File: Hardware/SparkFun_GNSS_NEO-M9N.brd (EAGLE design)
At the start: 64.9 x 38 mm, 68 parts, among them J1 MICROMOD_STANDARD, U1 U-BLOX_NEO-M9N, U2 3.3V, U3 EEPROM, U4 74HC1G04

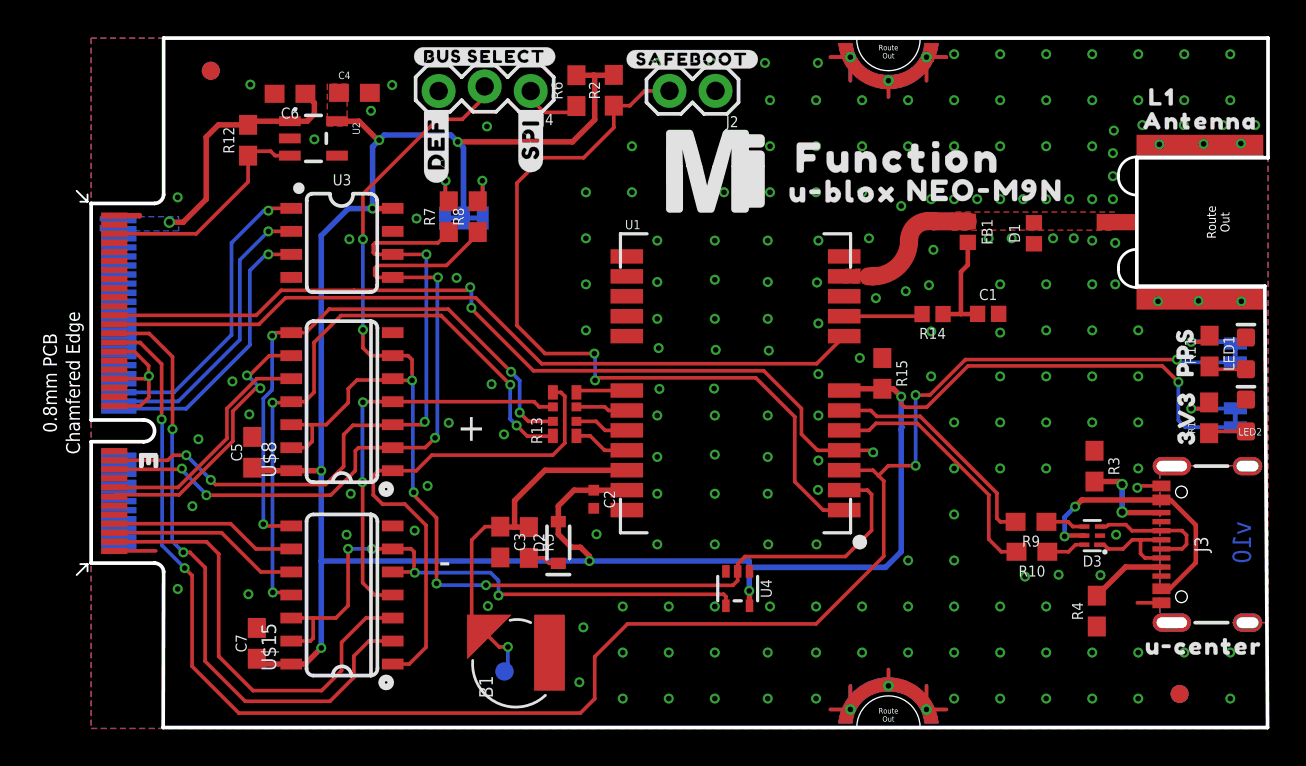
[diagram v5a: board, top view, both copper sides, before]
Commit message: Adds more text to clarify selection jumper, fixes some clearance issues and wire stubs
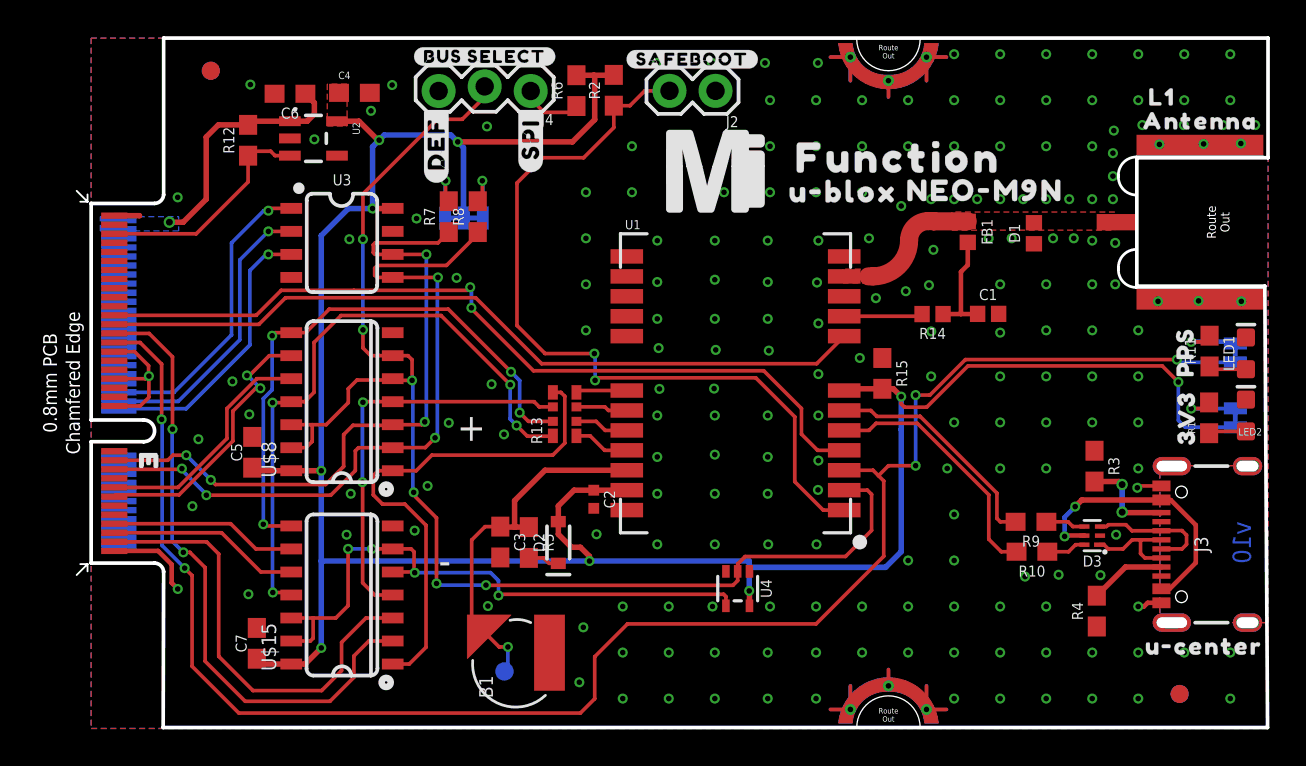
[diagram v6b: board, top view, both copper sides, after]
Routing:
- net GND: track 19.7 -> 22.4 mm, vias 205 -> 206
- net INT: track 48.0 -> 46.2 mm, vias 3 -> 2
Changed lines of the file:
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@@
 <layer number="115" name="ReferenceISLANDS" color="7" fill="1" visible="no" active="no"/>
 <layer number="116" name="Patch_BOT" color="9" fill="4" visible="no" active="no"/>
-<layer number="117" name="PM_Ref" color="26" fill="1" visible="no" active="yes"/>
+<layer number="117" name="PM_Ref" color="26" fill="1" visible="yes" active="yes"/>
 <layer number="118" name="Rect_Pads" color="7" fill="1" visible="no" active="no"/>
-<layer number="119" name="PF_Ref" color="31" fill="1" visible="no" active="yes"/>
-<layer number="120" name="WFL_Ref" color="25" fill="1" visible="no" active="yes"/>
+<layer number="119" name="PF_Ref" color="31" fill="1" visible="yes" active="yes"/>
+<layer number="120" name="WFL_Ref" color="25" fill="1" visible="yes" active="yes"/>
 <layer number="121" name="_tsilk" color="7" fill="1" visible="no" active="no"/>
 <layer number="122" name="_bsilk" color="7" fill="1" visible="no" active="no"/>
@@
 <wire x1="25.781" y1="11.413" x2="25.781" y2="12.281" width="0.3048" layer="1"/>
 <wire x1="25.781" y1="12.281" x2="26.6492" y2="13.1492" width="0.3048" layer="1"/>
-<wire x1="44.8283" y1="16.6243" x2="44.704" y2="16.5" width="0.2032" layer="16"/>
 <wire x1="12.7" y1="14.224" x2="12.7" y2="27.2" width="0.3048" layer="16"/>
 <wire x1="14.192" y1="28.692" x2="15.53" y2="28.692" width="0.3048" layer="16"/>
@@
 <wire x1="57.835" y1="13.385" x2="57.7342" y2="13.2842" width="0.2032" layer="1"/>
 <wire x1="59.0648" y1="6.935" x2="59.064" y2="6.9342" width="0.2032" layer="1"/>
-<wire x1="59.064" y1="6.9342" x2="57.7342" y2="6.9342" width="0.2032" layer="1"/>
 <via x="31.2166" y="36.7284" extent="1-16" drill="0.3048"/>
 <via x="40.005" y="4.191" extent="1-16" drill="0.3048"/>
@@
 <contactref element="C7" pad="2"/>
 <via x="8.727" y="17.3344" extent="1-16" drill="0.3048"/>
-<wire x1="1.275" y1="9.8" x2="3.5684" y2="9.8" width="0.2032" layer="1"/>
 <via x="8.679" y="7.4094" extent="1-16" drill="0.3048"/>
 <via x="37.398" y="20.852" extent="1-16" drill="0.3048"/>
@@
 <via x="52.705" y="6.731" extent="1-16" drill="0.3048"/>
 <via x="42.545" y="6.731" extent="1-16" drill="0.3048"/>
-<via x="47.625" y="14.351" extent="1-16" drill="0.3048"/>
+<via x="47.244" y="14.351" extent="1-16" drill="0.3048"/>
 <via x="47.625" y="16.891" extent="1-16" drill="0.3048"/>
 <via x="50.165" y="16.891" extent="1-16" drill="0.3048"/>
@@
 <via x="40.005" y="6.731" extent="1-16" drill="0.3048"/>
 <via x="37.465" y="6.731" extent="1-16" drill="0.3048"/>
-<via x="34.417" y="6.731" extent="1-16" drill="0.3048"/>
+<via x="34.29" y="6.731" extent="1-16" drill="0.3048"/>
 <via x="31.877" y="1.651" extent="1-16" drill="0.3048"/>
 <via x="31.877" y="4.191" extent="1-16" drill="0.3048"/>
@@
 <via x="27.305" y="24.511" extent="1-16" drill="0.3048"/>
 <via x="27.305" y="21.971" extent="1-16" drill="0.3048"/>
+<via x="57.785" y="6.731" extent="1-16" drill="0.3048"/>
+<wire x1="59.0648" y1="6.935" x2="58.3028" y2="6.935" width="0.254" layer="1"/>
+<wire x1="58.3028" y1="6.935" x2="58.0988" y2="6.731" width="0.254" layer="1"/>
+<wire x1="58.0988" y1="6.731" x2="57.785" y2="6.731" width="0.254" layer="1"/>
+<wire x1="4.779" y1="7.6994" x2="4.445" y2="8.0334" width="0.254" layer="1"/>
+<wire x1="4.445" y1="9.0504" x2="3.6954" y2="9.8" width="0.254" layer="1"/>
+<wire x1="4.445" y1="8.0334" x2="4.445" y2="9.0504" width="0.254" layer="1"/>
+<wire x1="3.6954" y1="9.8" x2="1.275" y2="9.8" width="0.254" layer="1"/>
 </signal>
 <signal name="SCL/SCK">
 <contactref element="R13" pad="P6"/>
-<wire x1="25.4502" y1="17.78" x2="25.482" y2="17.7482" width="0.2032" layer="1"/>
 <contactref element="U$8" pad="4"/>
 <contactref element="U$15" pad="4"/>
@@
 <contactref element="U1" pad="8"/>
 <contactref element="J1" pad="51"/>
-<wire x1="41.56" y1="21.65" x2="41.627" y2="21.717" width="0.2032" layer="1"/>
 <wire x1="1.275" y1="22.3" x2="9.26" y2="22.3" width="0.2032" layer="1"/>
 <wire x1="9.26" y1="22.3" x2="10.73" y2="23.77" width="0.2032" layer="1"/>
@@
 <signal name="INT">
 <contactref element="U1" pad="4"/>
-<wire x1="43.307" y1="15.0876" x2="43.1546" y2="15.24" width="0.2032" layer="16"/>
-<via x="43.1546" y="15.24" extent="1-16" drill="0.3048"/>
 <contactref element="J1" pad="53"/>
-<wire x1="41.56" y1="15.35" x2="43.0446" y2="15.35" width="0.2032" layer="1"/>
-<wire x1="43.0446" y1="15.35" x2="43.1546" y2="15.24" width="0.2032" layer="1"/>
 <wire x1="1.275" y1="22.8" x2="9.11" y2="22.8" width="0.2032" layer="1"/>
 <wire x1="9.11" y1="22.8" x2="10.49" y2="24.18" width="0.2032" layer="1"/>
@@
 <wire x1="47.014" y1="22.87" x2="48" y2="22.87" width="0.254" layer="1"/>
 <wire x1="48" y1="22.87" x2="48.9116" y2="22.87" width="0.254" layer="1"/>
-<wire x1="48.3774" y1="26.8264" x2="48.482" y2="26.7218" width="0.254" layer="1"/>
 <wire x1="48.9216" y1="22.88" x2="48.9116" y2="22.87" width="0.254" layer="1"/>
 <wire x1="48.3774" y1="25.5774" x2="48.3774" y2="26.8264" width="0.254" layer="1"/>
@@
 <wire x1="23.368" y1="12.573" x2="23.368" y2="11.113" width="0.3048" layer="1"/>
 <wire x1="25.045" y1="14.25" x2="23.368" y2="12.573" width="0.3048" layer="1"/>
-<wire x1="22.5806" y1="11.1384" x2="22.719" y2="11.2768" width="0.3048" layer="1"/>
 <wire x1="21.4122" y1="5.6034" x2="21" y2="6.0156" width="0.2032" layer="1"/>
 <wire x1="21" y1="6.0156" x2="21" y2="10.4" width="0.2032" layer="1"/>
@@
 <wire x1="16.737" y1="19.21" x2="16.717" y2="19.23" width="0.2032" layer="1"/>
 <wire x1="16.717" y1="19.23" x2="16.643" y2="19.304" width="0.2032" layer="1"/>
-<wire x1="16.643" y1="20.56" x2="16.643" y2="20.574" width="0.2032" layer="1"/>
 <wire x1="11.043" y1="16.764" x2="12.2" y2="16.764" width="0.2032" layer="1"/>
 <wire x1="12.2" y1="16.764" x2="12.974" y2="16.764" width="0.2032" layer="1"/>
@@
 <wire x1="18.44" y1="15.5" x2="18.98" y2="16.04" width="0.2032" layer="1"/>
 <via x="18.98" y="16.04" extent="1-16" drill="0.3048"/>
-<wire x1="21.4308" y1="27.3" x2="21.3936" y2="27.3372" width="0.2032" layer="1"/>
 <wire x1="21.3936" y1="27.3372" x2="21.336" y2="27.3948" width="0.2032" layer="1"/>
 <wire x1="18.98" y1="16.04" x2="19.107" y2="16.167" width="0.2032" layer="16"/>
@@
 <via x="18.41" y="16.92" extent="1-16" drill="0.3048"/>
 <wire x1="18.41" y1="16.92" x2="18.5" y2="17.01" width="0.2032" layer="16"/>
-<wire x1="19.5" y1="27.5" x2="19.6705" y2="27.3295" width="0.2032" layer="1"/>
 <wire x1="18.5" y1="26.159" x2="18.503" y2="26.162" width="0.2032" layer="16"/>
 <via x="18.503" y="26.162" extent="1-16" drill="0.3048"/>
@@
 <via x="14.18" y="9.91" extent="1-16" drill="0.3048"/>
 <wire x1="12.25" y1="6.096" x2="13.5" y2="6.096" width="0.2032" layer="1"/>
-<wire x1="15.48" y1="9.91" x2="15.5" y2="9.91" width="0.2032" layer="1"/>
 <wire x1="15.5" y1="9.91" x2="16.639" y2="9.91" width="0.2032" layer="1"/>
 <wire x1="16.639" y1="9.91" x2="16.643" y2="9.906" width="0.2032" layer="1"/>

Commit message: Adds some vias, moves some silk
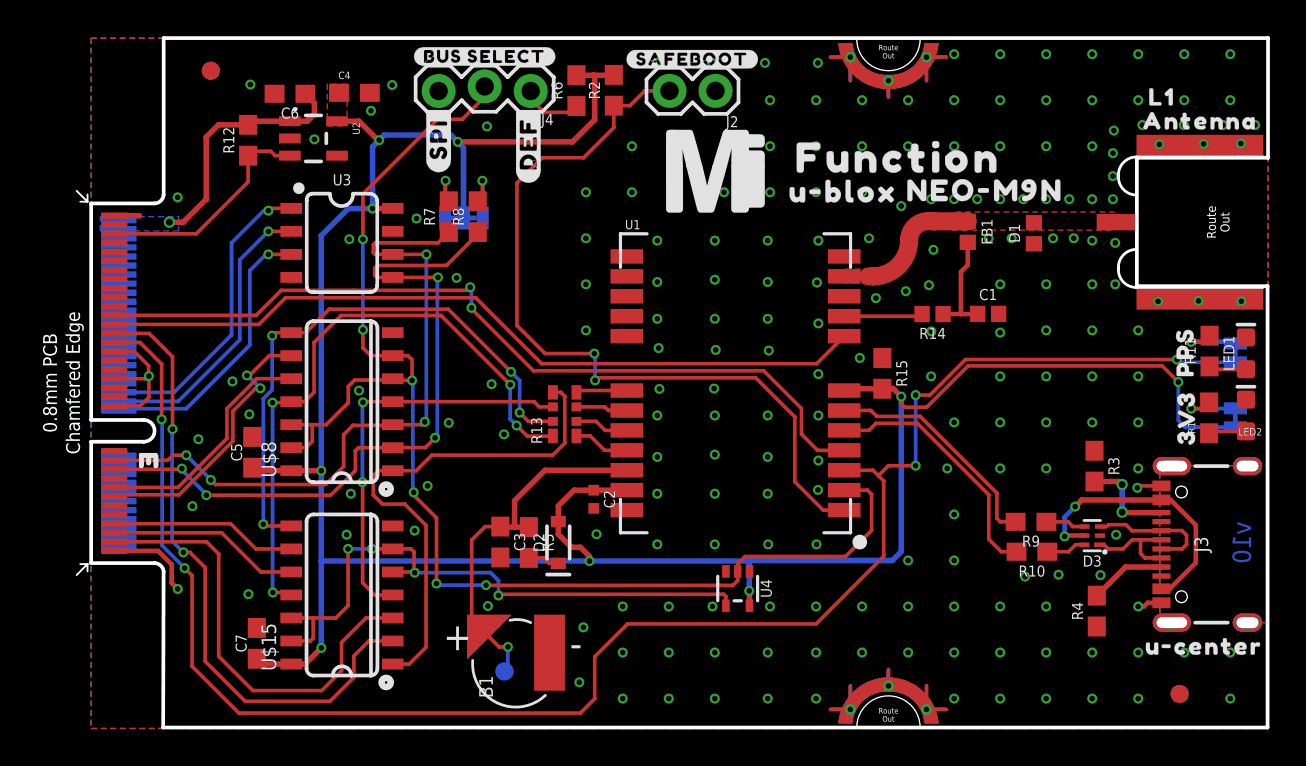
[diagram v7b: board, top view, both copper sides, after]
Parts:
- moved U$17 5.08 mm to (19.2, 32.5)
- moved U$16 5.08 mm to (24.1, 32.3)
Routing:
- net GND: vias 206 -> 207
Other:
- outline, holes or cut-outs redrawn
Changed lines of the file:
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@@
 <?xml version="1.0" encoding="utf-8"?>
 <!DOCTYPE eagle SYSTEM "eagle.dtd">
-<eagle version="9.6.2">
+<eagle version="9.5.1">
 <drawing>
 <settings>
@@
 <layer number="45" name="Holes" color="7" fill="1" visible="yes" active="yes"/>
 <layer number="46" name="Milling" color="3" fill="1" visible="no" active="yes"/>
-<layer number="47" name="Measures" color="7" fill="1" visible="no" active="yes"/>
+<layer number="47" name="Measures" color="7" fill="1" visible="yes" active="yes"/>
 <layer number="48" name="Document" color="7" fill="1" visible="no" active="yes"/>
 <layer number="49" name="Reference" color="13" fill="1" visible="yes" active="yes"/>
@@
 <layer number="115" name="ReferenceISLANDS" color="7" fill="1" visible="no" active="no"/>
 <layer number="116" name="Patch_BOT" color="9" fill="4" visible="no" active="no"/>
-<layer number="117" name="PM_Ref" color="26" fill="1" visible="yes" active="yes"/>
+<layer number="117" name="PM_Ref" color="26" fill="1" visible="no" active="yes"/>
 <layer number="118" name="Rect_Pads" color="7" fill="1" visible="no" active="no"/>
-<layer number="119" name="PF_Ref" color="31" fill="1" visible="yes" active="yes"/>
-<layer number="120" name="WFL_Ref" color="25" fill="1" visible="yes" active="yes"/>
+<layer number="119" name="PF_Ref" color="31" fill="1" visible="no" active="yes"/>
+<layer number="120" name="WFL_Ref" color="25" fill="1" visible="no" active="yes"/>
 <layer number="121" name="_tsilk" color="7" fill="1" visible="no" active="no"/>
 <layer number="122" name="_bsilk" color="7" fill="1" visible="no" active="no"/>
@@
 <wire x1="64.9478" y1="31.496" x2="57.7088" y2="31.496" width="0.2032" layer="20"/>
 <wire x1="57.7088" y1="31.496" x2="57.7088" y2="24.4094" width="0.2032" layer="20"/>
-<wire x1="57.7088" y1="24.4094" x2="64.77" y2="24.4094" width="0.2032" layer="20"/>
+<wire x1="57.7088" y1="24.4094" x2="64.9224" y2="24.4094" width="0.2032" layer="20"/>
 <wire x1="64.9478" y1="31.496" x2="64.9478" y2="38.1" width="0.2032" layer="20"/>
-<wire x1="64.77" y1="24.4094" x2="64.9224" y2="0.0508" width="0.2032" layer="20"/>
+<wire x1="64.9224" y1="24.4094" x2="64.9224" y2="0.0508" width="0.2032" layer="20"/>
 <text x="88.5" y="40" size="1.778" layer="51" font="vector" ratio="15">0.8mm PCB
 45 degree chamfered edge
@@
 <dimension x1="64.9424" y1="27.94" x2="64.9478" y2="38.1" x3="74.673896875" y3="33.014828125" textsize="1.778" textratio="15" layer="47" unit="inch"/>
 <text x="64.008" y="11.43" size="1.016" layer="16" font="vector" ratio="15" rot="SMR270">v10</text>
-<text x="20.193" y="15.875" size="1.524" layer="21" font="vector" ratio="15">+</text>
-<text x="19.177" y="8.509" size="1.524" layer="21" font="vector" ratio="15">-</text>
+<text x="19.431" y="4.318" size="1.524" layer="21" font="vector" ratio="15">+</text>
+<text x="26.416" y="3.937" size="1.524" layer="21" font="vector" ratio="15">-</text>
 <dimension x1="58.7248" y1="10.16" x2="58.674" y2="0" x3="72.161125" y3="5.012690625" textsize="1.778" textratio="15" layer="47" unit="inch"/>
 <dimension x1="4" y1="38.1" x2="43.942" y2="38.1" x3="23.971" y3="41.656" textsize="1.778" textratio="15" layer="47" unit="inch"/>
@@
 <attribute name="REV" value="" x="1.27" y="-39.37" size="1.778" layer="27" font="vector" ratio="15" display="off"/>
 </element>
-<element name="U$16" library="top" package="#DEF#521" value="" x="19.05" y="32.258" smashed="yes" rot="R90"/>
-<element name="U$17" library="top" package="#SPI#520" value="" x="24.257" y="32.512" smashed="yes" rot="R90"/>
+<element name="U$16" library="top" package="#DEF#521" value="" x="24.13" y="32.258" smashed="yes" rot="R90"/>
+<element name="U$17" library="top" package="#SPI#520" value="" x="19.177" y="32.512" smashed="yes" rot="R90"/>
 <element name="U$18" library="top" package="#BUS_SELECT#509" value="" x="21.717" y="37.084" smashed="yes"/>
 </elements>
@@
 <wire x1="43.6638" y1="18.745" x2="44.2724" y2="18.745" width="0.3048" layer="1"/>
 <wire x1="44.2724" y1="18.745" x2="44.704" y2="18.3134" width="0.3048" layer="1"/>
-<wire x1="44.704" y1="18.3134" x2="44.704" y2="16.5" width="0.3048" layer="16"/>
 <contactref element="U4" pad="5"/>
 <contactref element="U$8" pad="14"/>
@@
 <contactref element="U$15" pad="14"/>
 <contactref element="C7" pad="1"/>
-<wire x1="44.704" y1="16.5" x2="44.704" y2="9.7536" width="0.3048" layer="16"/>
+<wire x1="44.704" y1="18.3134" x2="44.704" y2="9.7536" width="0.3048" layer="16"/>
 <wire x1="11.043" y1="3.556" x2="11.811" y2="3.556" width="0.3048" layer="1"/>
 <wire x1="11.811" y1="3.556" x2="12.7" y2="4.445" width="0.3048" layer="1"/>
@@
 <wire x1="20.2311" y1="32.3723" x2="26.5623" y2="32.3723" width="0.3048" layer="1"/>
 <via x="20.2311" y="32.3723" extent="1-16" drill="0.3048"/>
-<wire x1="44.704" y1="9.7536" x2="43.8404" y2="8.89" width="0.3048" layer="16"/>
-<wire x1="43.8404" y1="8.89" x2="36.315" y2="8.89" width="0.3048" layer="16"/>
+<wire x1="44.704" y1="9.7536" x2="44.2214" y2="9.271" width="0.3048" layer="16"/>
+<wire x1="44.2214" y1="9.271" x2="36.315" y2="9.271" width="0.3048" layer="16"/>
 <wire x1="36.315" y1="9.24" x2="27.5" y2="9.24" width="0.3048" layer="16"/>
 <wire x1="27.5" y1="9.24" x2="12.7" y2="9.24" width="0.3048" layer="16"/>
@@
 <wire x1="36.33" y1="7.578" x2="36.315" y2="7.593" width="0.3048" layer="1"/>
 <via x="36.315" y="7.593" extent="1-16" drill="0.3048"/>
-<wire x1="36.315" y1="7.593" x2="36.315" y2="8.89" width="0.3048" layer="16"/>
-<wire x1="36.315" y1="8.89" x2="36.315" y2="9.24" width="0.3048" layer="16"/>
+<wire x1="36.315" y1="7.593" x2="36.315" y2="9.144" width="0.3048" layer="16"/>
+<wire x1="36.315" y1="9.24" x2="36.315" y2="9.271" width="0.3048" layer="16"/>
+<wire x1="36.315" y1="9.144" x2="36.315" y2="9.24" width="0.3048" layer="16"/>
 <wire x1="26.6492" y1="13.1492" x2="27.7368" y2="13.1492" width="0.3048" layer="1"/>
 <wire x1="25.781" y1="11.413" x2="25.781" y2="12.281" width="0.3048" layer="1"/>
@@
 <wire x1="4.445" y1="8.0334" x2="4.445" y2="9.0504" width="0.254" layer="1"/>
 <wire x1="3.6954" y1="9.8" x2="1.275" y2="9.8" width="0.254" layer="1"/>
+<via x="14.7828" y="18.6436" extent="1-16" drill="0.3048"/>
 </signal>
 <signal name="SCL/SCK">
@@
 <wire x1="11.043" y1="16.764" x2="12.2" y2="16.764" width="0.2032" layer="1"/>
 <wire x1="12.2" y1="16.764" x2="12.974" y2="16.764" width="0.2032" layer="1"/>
-<wire x1="14.19" y1="17.98" x2="14.19" y2="18.75" width="0.2032" layer="1"/>
-<wire x1="14.19" y1="18.75" x2="14.67" y2="19.23" width="0.2032" layer="1"/>
-<wire x1="14.67" y1="19.23" x2="16.717" y2="19.23" width="0.2032" layer="1"/>
+<wire x1="14.19" y1="17.98" x2="14.19" y2="18.877" width="0.2032" layer="1"/>
+<wire x1="14.19" y1="18.877" x2="14.543" y2="19.23" width="0.2032" layer="1"/>
+<wire x1="14.543" y1="19.23" x2="16.717" y2="19.23" width="0.2032" layer="1"/>
 <wire x1="12.974" y1="16.764" x2="14.19" y2="17.98" width="0.2032" layer="1"/>
 <wire x1="35.68" y1="9.08" x2="36.09" y2="9.49" width="0.2032" layer="1"/>
